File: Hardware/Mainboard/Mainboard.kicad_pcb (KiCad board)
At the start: 4 copper layers, 185.4 x 160 mm, 60 parts, among them IC1 TUSB2046BIRHBR, IC2 TUSB2046BIRHBR, IC3 TUSB2046BIRHBR, IC4 AOZ2261NQI-11, J1 Conn_02x10_Odd_Even, J10 Conn_02x03_Counter_Clockwise, J11 Conn_02x03_Counter_Clockwise, J12 ARJM11D7-009-AB-EW2, J13 USB4105-GF-A-060, J14 Conn_02x03_Odd_Even, J15 Conn_02x03_Odd_Even, J16 1844210, J17 Conn_02x03_Counter_Clockwise, J18 Conn_02x03_Counter_Clockwise, J19 Conn_02x03_Counter_Clockwise, J2 Conn_02x10_Odd_Even, J20 Conn_02x03_Counter_Clockwise, J21 Conn_02x03_Counter_Clockwise, J22 Conn_02x03_Counter_Clockwise, J23 Conn_02x03_Counter_Clockwise, J3 Conn_02x10_Odd_Even, J4 Conn_02x10_Odd_Even, J5 Conn_02x10_Odd_Even, J6 Conn_02x10_Odd_Even, J7 Conn_02x10_Odd_Even, J8 Conn_02x08_Odd_Even, J9 Conn_02x12_Odd_Even, P1 USB-A1HSW6, P2 USB-A1HSW6, SW1 SW_Push_Dual, SW2 SW_Push_Dual, SW3 SW_DPST, U1 ENC624J600-I/PT, U2 SC0915, U3 CD74HC154M96, U4 TCA9548A, U5 AZ1084CD-3.3TRG1, U6 AZ1084CD-3.3TRG1

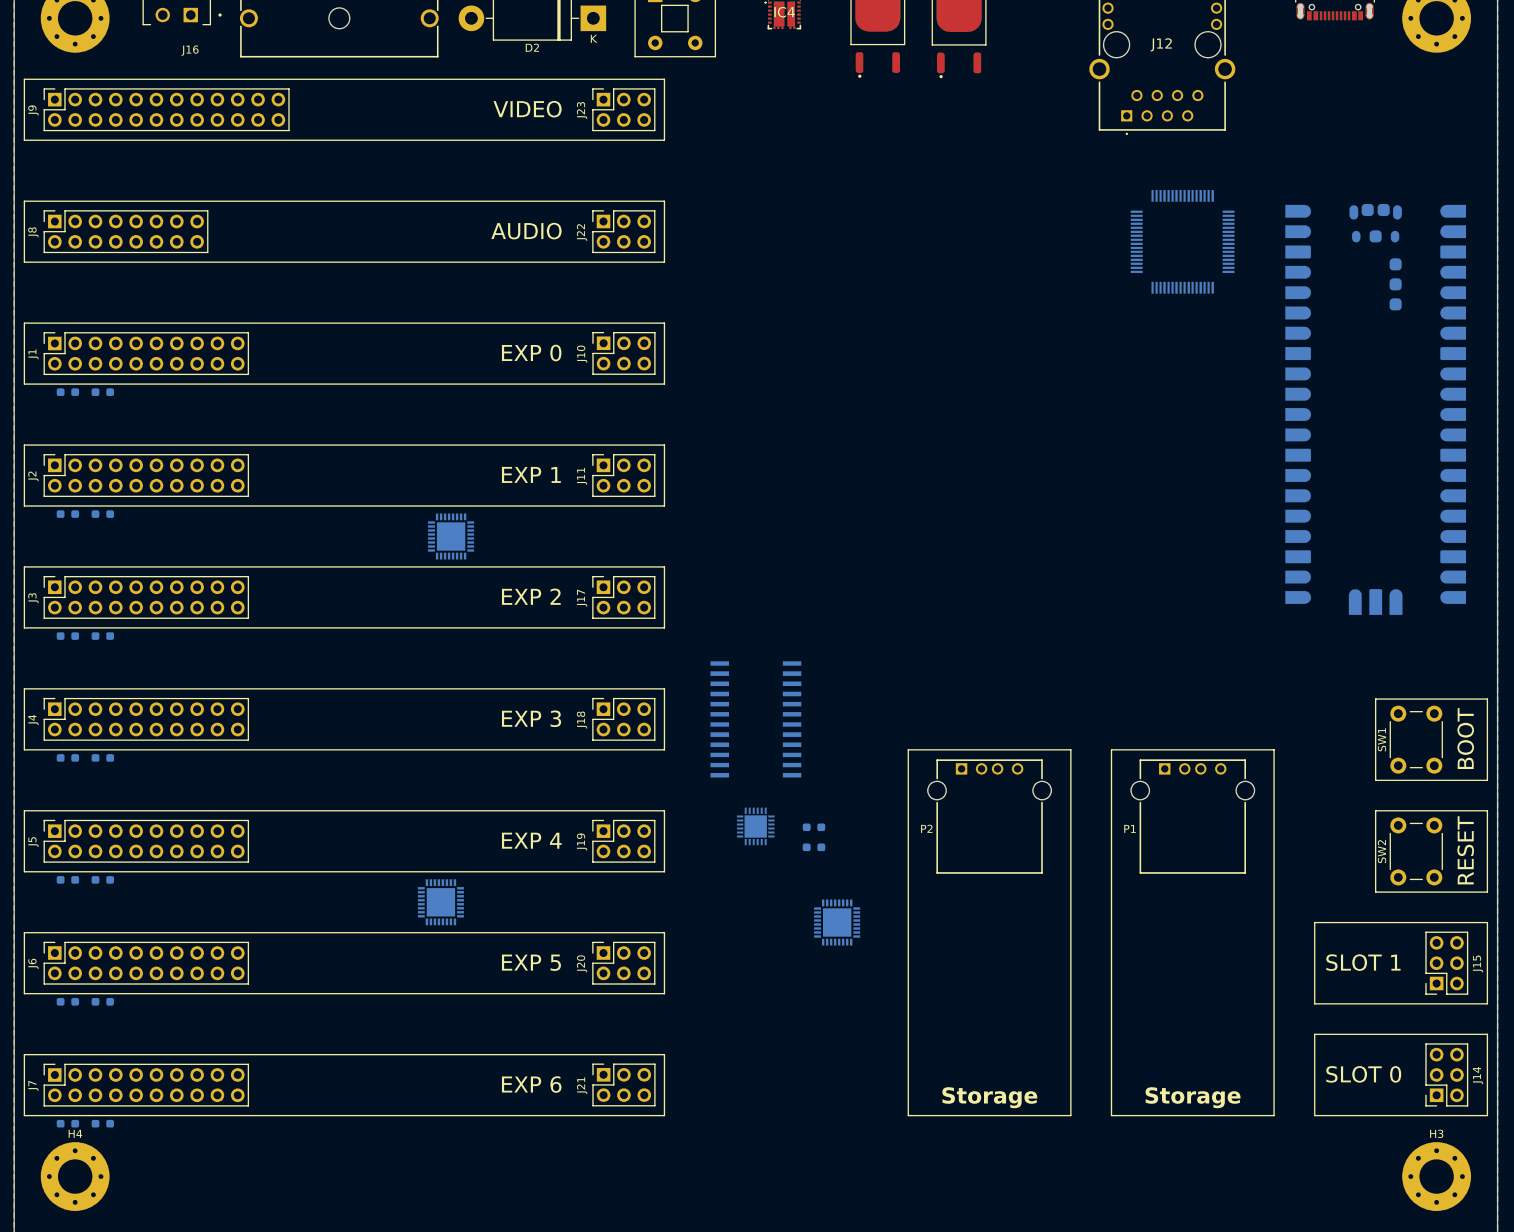
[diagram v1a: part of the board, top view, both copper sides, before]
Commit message: Adds RP2350 Stamp XL and dummy expansion board
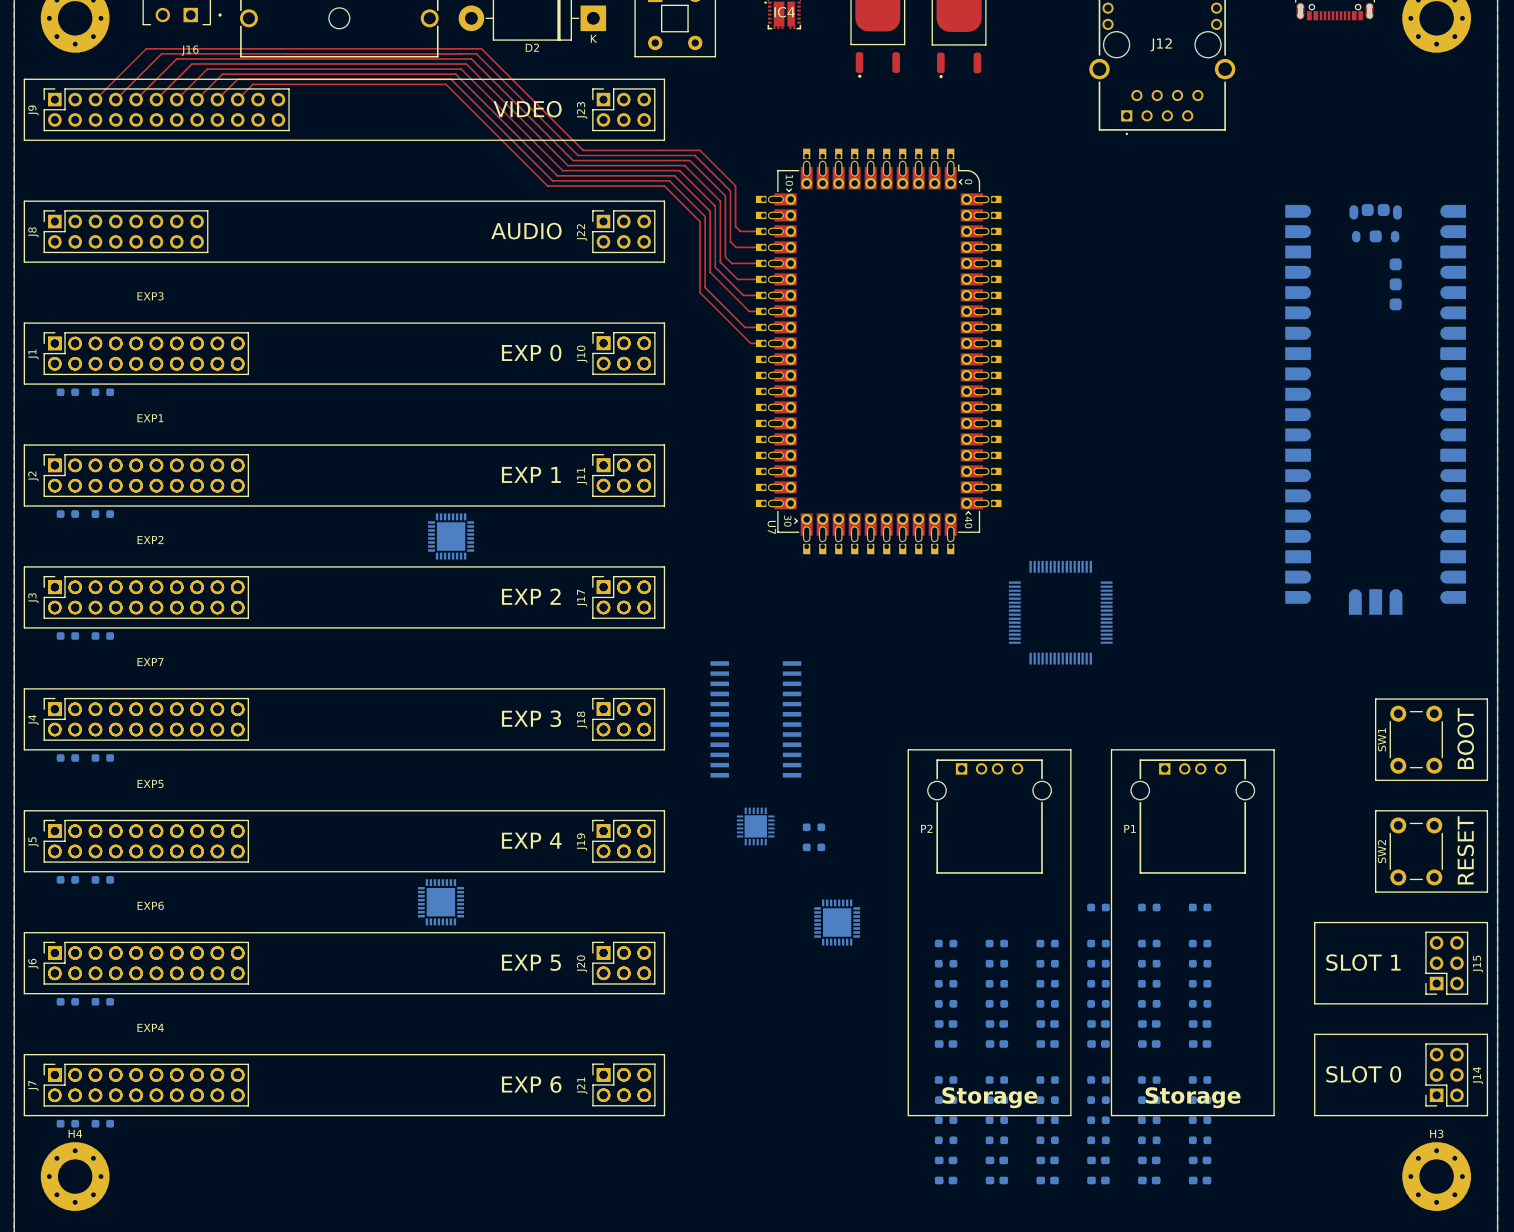
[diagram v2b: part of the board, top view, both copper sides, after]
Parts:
- added C1: 22pF, Capacitor_SMD:C_0603_1608Metric_Pad1.08x0.95mm_HandSolder, B.Cu at (159.7, 185.9)
- added C10: 22pF, Capacitor_SMD:C_0603_1608Metric_Pad1.08x0.95mm_HandSolder, B.Cu at (166.0, 166.3)
- added C11: 22pF, Capacitor_SMD:C_0603_1608Metric_Pad1.08x0.95mm_HandSolder, B.Cu at (191.4, 185.9)
- added C12: 22pF, Capacitor_SMD:C_0603_1608Metric_Pad1.08x0.95mm_HandSolder, B.Cu at (191.4, 183.4)
- added C13: 22pF, Capacitor_SMD:C_0603_1608Metric_Pad1.08x0.95mm_HandSolder, B.Cu at (185.1, 168.8)
- added C14: 22pF, Capacitor_SMD:C_0603_1608Metric_Pad1.08x0.95mm_HandSolder, B.Cu at (185.1, 166.3)
- added C15: 22pF, Capacitor_SMD:C_0603_1608Metric_Pad1.08x0.95mm_HandSolder, B.Cu at (166.0, 185.9)
- added C16: 22pF, Capacitor_SMD:C_0603_1608Metric_Pad1.08x0.95mm_HandSolder, B.Cu at (166.0, 183.4)
- added C17: 22pF, Capacitor_SMD:C_0603_1608Metric_Pad1.08x0.95mm_HandSolder, B.Cu at (185.1, 185.9)
- added C18: 22pF, Capacitor_SMD:C_0603_1608Metric_Pad1.08x0.95mm_HandSolder, B.Cu at (185.1, 183.4)
- added C19: 22pF, Capacitor_SMD:C_0603_1608Metric_Pad1.08x0.95mm_HandSolder, B.Cu at (178.7, 168.8)
- added C2: 22pF, Capacitor_SMD:C_0603_1608Metric_Pad1.08x0.95mm_HandSolder, B.Cu at (172.4, 168.8)
- added C20: 22pF, Capacitor_SMD:C_0603_1608Metric_Pad1.08x0.95mm_HandSolder, B.Cu at (178.7, 166.3)
- added C21: 22pF, Capacitor_SMD:C_0603_1608Metric_Pad1.08x0.95mm_HandSolder, B.Cu at (159.7, 168.8)
- added C22: 22pF, Capacitor_SMD:C_0603_1608Metric_Pad1.08x0.95mm_HandSolder, B.Cu at (159.7, 166.3)
- added C23: 22pF, Capacitor_SMD:C_0603_1608Metric_Pad1.08x0.95mm_HandSolder, B.Cu at (178.7, 185.9)
- added C24: 22pF, Capacitor_SMD:C_0603_1608Metric_Pad1.08x0.95mm_HandSolder, B.Cu at (178.7, 183.4)
- added C3: 22pF, Capacitor_SMD:C_0603_1608Metric_Pad1.08x0.95mm_HandSolder, B.Cu at (172.4, 185.9)
- added C4: 22pF, Capacitor_SMD:C_0603_1608Metric_Pad1.08x0.95mm_HandSolder, B.Cu at (159.7, 183.4)
- added C5: 22pF, Capacitor_SMD:C_0603_1608Metric_Pad1.08x0.95mm_HandSolder, B.Cu at (172.4, 166.3)
- added C6: 22pF, Capacitor_SMD:C_0603_1608Metric_Pad1.08x0.95mm_HandSolder, B.Cu at (172.4, 183.4)
- added C7: 22pF, Capacitor_SMD:C_0603_1608Metric_Pad1.08x0.95mm_HandSolder, B.Cu at (191.4, 168.8)
- added C8: 22pF, Capacitor_SMD:C_0603_1608Metric_Pad1.08x0.95mm_HandSolder, B.Cu at (191.4, 166.3)
- added C9: 22pF, Capacitor_SMD:C_0603_1608Metric_Pad1.08x0.95mm_HandSolder, B.Cu at (166.0, 168.8)
- added EXP1: ~, Home Computer:Expansion Card Preview, F.Cu at (59.7, 97.8)
- added EXP2: ~, Home Computer:Expansion Card Preview, F.Cu at (59.7, 113.0)
- added EXP3: ~, Home Computer:Expansion Card Preview, F.Cu at (59.7, 82.5)
- added EXP4: ~, Home Computer:Expansion Card Preview, F.Cu at (59.7, 174.0)
- added EXP5: ~, Home Computer:Expansion Card Preview, F.Cu at (59.7, 143.5)
- added EXP6: ~, Home Computer:Expansion Card Preview, F.Cu at (59.7, 158.7)
- added EXP7: ~, Home Computer:Expansion Card Preview, F.Cu at (59.7, 128.3)
- added R17: 10K, Resistor_SMD:R_0603_1608Metric_Pad0.98x0.95mm_HandSolder, B.Cu at (178.7, 151.8)
- added R18: 10K, Resistor_SMD:R_0603_1608Metric_Pad0.98x0.95mm_HandSolder, B.Cu at (191.4, 151.8)
- added R19: 10K, Resistor_SMD:R_0603_1608Metric_Pad0.98x0.95mm_HandSolder, B.Cu at (185.1, 151.8)
- added R20: 27, Resistor_SMD:R_0603_1608Metric_Pad0.98x0.95mm_HandSolder, B.Cu at (159.7, 180.9)
- added R21: 27, Resistor_SMD:R_0603_1608Metric_Pad0.98x0.95mm_HandSolder, B.Cu at (159.7, 178.4)
- added R22: 27, Resistor_SMD:R_0603_1608Metric_Pad0.98x0.95mm_HandSolder, B.Cu at (172.4, 163.8)
- added R23: 27, Resistor_SMD:R_0603_1608Metric_Pad0.98x0.95mm_HandSolder, B.Cu at (172.4, 161.3)
- added R24: 27, Resistor_SMD:R_0603_1608Metric_Pad0.98x0.95mm_HandSolder, B.Cu at (172.4, 180.9)
- added R25: 27, Resistor_SMD:R_0603_1608Metric_Pad0.98x0.95mm_HandSolder, B.Cu at (172.4, 178.4)
- added R26: 27, Resistor_SMD:R_0603_1608Metric_Pad0.98x0.95mm_HandSolder, B.Cu at (191.4, 163.8)
- added R27: 27, Resistor_SMD:R_0603_1608Metric_Pad0.98x0.95mm_HandSolder, B.Cu at (191.4, 161.3)
- added R28: 15K, Resistor_SMD:R_0603_1608Metric_Pad0.98x0.95mm_HandSolder, B.Cu at (191.4, 158.8)
- added R29: 15K, Resistor_SMD:R_0603_1608Metric_Pad0.98x0.95mm_HandSolder, B.Cu at (191.4, 156.3)
- added R30: 27, Resistor_SMD:R_0603_1608Metric_Pad0.98x0.95mm_HandSolder, B.Cu at (166.0, 163.8)
- added R31: 27, Resistor_SMD:R_0603_1608Metric_Pad0.98x0.95mm_HandSolder, B.Cu at (166.0, 161.3)
- added R32: 27, Resistor_SMD:R_0603_1608Metric_Pad0.98x0.95mm_HandSolder, B.Cu at (178.7, 163.8)
- added R33: 27, Resistor_SMD:R_0603_1608Metric_Pad0.98x0.95mm_HandSolder, B.Cu at (178.7, 161.3)
- added R34: 15K, Resistor_SMD:R_0603_1608Metric_Pad0.98x0.95mm_HandSolder, B.Cu at (178.7, 158.8)
- added R35: 15K, Resistor_SMD:R_0603_1608Metric_Pad0.98x0.95mm_HandSolder, B.Cu at (178.7, 156.3)
- added R36: 27, Resistor_SMD:R_0603_1608Metric_Pad0.98x0.95mm_HandSolder, B.Cu at (159.7, 163.8)
- added R37: 27, Resistor_SMD:R_0603_1608Metric_Pad0.98x0.95mm_HandSolder, B.Cu at (159.7, 161.3)
- added R38: 15K, Resistor_SMD:R_0603_1608Metric_Pad0.98x0.95mm_HandSolder, B.Cu at (159.7, 158.8)
- added R39: 15K, Resistor_SMD:R_0603_1608Metric_Pad0.98x0.95mm_HandSolder, B.Cu at (159.7, 156.3)
- added R40: 27, Resistor_SMD:R_0603_1608Metric_Pad0.98x0.95mm_HandSolder, B.Cu at (178.7, 180.9)
- added R41: 27, Resistor_SMD:R_0603_1608Metric_Pad0.98x0.95mm_HandSolder, B.Cu at (178.7, 178.4)
- added R42: 15K, Resistor_SMD:R_0603_1608Metric_Pad0.98x0.95mm_HandSolder, B.Cu at (178.7, 175.9)
- added R43: 15K, Resistor_SMD:R_0603_1608Metric_Pad0.98x0.95mm_HandSolder, B.Cu at (178.7, 173.4)
- added R44: 15K, Resistor_SMD:R_0603_1608Metric_Pad0.98x0.95mm_HandSolder, B.Cu at (159.7, 175.9)
- added R45: 15K, Resistor_SMD:R_0603_1608Metric_Pad0.98x0.95mm_HandSolder, B.Cu at (172.4, 158.8)
- added R46: 15K, Resistor_SMD:R_0603_1608Metric_Pad0.98x0.95mm_HandSolder, B.Cu at (172.4, 175.9)
- added R47: 15K, Resistor_SMD:R_0603_1608Metric_Pad0.98x0.95mm_HandSolder, B.Cu at (159.7, 173.4)
- added R48: 15K, Resistor_SMD:R_0603_1608Metric_Pad0.98x0.95mm_HandSolder, B.Cu at (172.4, 156.3)
- added R49: 15K, Resistor_SMD:R_0603_1608Metric_Pad0.98x0.95mm_HandSolder, B.Cu at (172.4, 173.4)
- added R50: 15K, Resistor_SMD:R_0603_1608Metric_Pad0.98x0.95mm_HandSolder, B.Cu at (166.0, 158.8)
- added R51: 15K, Resistor_SMD:R_0603_1608Metric_Pad0.98x0.95mm_HandSolder, B.Cu at (166.0, 156.3)
- added R52: 27, Resistor_SMD:R_0603_1608Metric_Pad0.98x0.95mm_HandSolder, B.Cu at (191.4, 180.9)
- added R53: 27, Resistor_SMD:R_0603_1608Metric_Pad0.98x0.95mm_HandSolder, B.Cu at (191.4, 178.4)
- added R54: 15K, Resistor_SMD:R_0603_1608Metric_Pad0.98x0.95mm_HandSolder, B.Cu at (191.4, 175.9)
- added R55: 15K, Resistor_SMD:R_0603_1608Metric_Pad0.98x0.95mm_HandSolder, B.Cu at (191.4, 173.4)
- added R56: 27, Resistor_SMD:R_0603_1608Metric_Pad0.98x0.95mm_HandSolder, B.Cu at (185.1, 163.8)
- added R57: 27, Resistor_SMD:R_0603_1608Metric_Pad0.98x0.95mm_HandSolder, B.Cu at (185.1, 161.3)
- added R58: 15K, Resistor_SMD:R_0603_1608Metric_Pad0.98x0.95mm_HandSolder, B.Cu at (185.1, 158.8)
- added R59: 15K, Resistor_SMD:R_0603_1608Metric_Pad0.98x0.95mm_HandSolder, B.Cu at (185.1, 156.3)
- added R60: 27, Resistor_SMD:R_0603_1608Metric_Pad0.98x0.95mm_HandSolder, B.Cu at (166.0, 180.9)
- added R61: 27, Resistor_SMD:R_0603_1608Metric_Pad0.98x0.95mm_HandSolder, B.Cu at (166.0, 178.4)
- added R62: 15K, Resistor_SMD:R_0603_1608Metric_Pad0.98x0.95mm_HandSolder, B.Cu at (166.0, 175.9)
- added R63: 15K, Resistor_SMD:R_0603_1608Metric_Pad0.98x0.95mm_HandSolder, B.Cu at (166.0, 173.4)
- added R64: 27, Resistor_SMD:R_0603_1608Metric_Pad0.98x0.95mm_HandSolder, B.Cu at (185.1, 180.9)
- added R65: 27, Resistor_SMD:R_0603_1608Metric_Pad0.98x0.95mm_HandSolder, B.Cu at (185.1, 178.4)
- added R66: 15K, Resistor_SMD:R_0603_1608Metric_Pad0.98x0.95mm_HandSolder, B.Cu at (185.1, 175.9)
- added R67: 15K, Resistor_SMD:R_0603_1608Metric_Pad0.98x0.95mm_HandSolder, B.Cu at (185.1, 173.4)
- added U7: RP2350_Stamp_XL, RP2xxx_Stamp:RP2xxx_Stamp_XL_FlexyPin, F.Cu at (151.2, 82.3)
- moved U1 48.8 mm to (174.0, 114.9), turned to 90 degrees
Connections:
- IC1 pad 10: unconnected-(IC1-~{OVRCUR}-Pad10) -> +3V3
- IC1 pad 11: /Expansion Subsystem/USB0_{D-} -> /Expansion Subsystem/USB Hub x5/USB Terminator3/HUB_{D-}
- IC1 pad 12: /Expansion Subsystem/USB0_{D+} -> /Expansion Subsystem/USB Hub x5/USB Terminator3/HUB_{D+}
- IC1 pad 14: unconnected-(IC1-~{OVRCUR2}-Pad14) -> +3V3
- IC1 pad 15: /Expansion Subsystem/USB1_{D-} -> /Expansion Subsystem/USB Hub x5/USB Terminator2/HUB_{D-}
- IC1 pad 16: /Expansion Subsystem/USB1_{D+} -> /Expansion Subsystem/USB Hub x5/USB Terminator2/HUB_{D+}
- IC1 pad 18: unconnected-(IC1-~{OVRCUR3}-Pad18) -> +3V3
- IC1 pad 19: /Expansion Subsystem/USB2_{D-} -> /Expansion Subsystem/USB Hub x5/USB Terminator1/HUB_{D-}
- IC1 pad 20: /Expansion Subsystem/USB2_{D+} -> /Expansion Subsystem/USB Hub x5/USB Terminator1/HUB_{D+}
- IC1 pad 22: unconnected-(IC1-~{OVRCUR4}-Pad22) -> +3V3
- IC1 pad 23: /Expansion Subsystem/USB3_{D-} -> /Expansion Subsystem/USB Hub x5/USB Terminator/HUB_{D-}
- IC1 pad 24: /Expansion Subsystem/USB3_{D+} -> /Expansion Subsystem/USB Hub x5/USB Terminator/HUB_{D+}
- IC1 pad 25: unconnected-(IC1-VCC_2-Pad25) -> +3V3
- IC1 pad 26: unconnected-(IC1-~{EXTMEM}-Pad26) -> +3V3
- IC1 pad 28: unconnected-(IC1-GND_2-Pad28) -> GND
- IC1 pad 3: unconnected-(IC1-VCC_1-Pad3) -> +3V3
- IC1 pad 33: unconnected-(IC1-EP-Pad33) -> GND
- IC1 pad 4: unconnected-(IC1-~{RESET}-Pad4) -> /Expansion Subsystem/USB Hub x5/~{RESET}
- IC1 pad 6: unconnected-(IC1-EEDATA/GANGED-Pad6) -> GND
- IC1 pad 7: unconnected-(IC1-GND_1-Pad7) -> GND
- IC1 pad 8: unconnected-(IC1-BUSPWR-Pad8) -> GND
- IC2 pad 10: unconnected-(IC2-~{OVRCUR}-Pad10) -> +3V3
- IC2 pad 11: /Expansion Subsystem/D0_{D+} -> /USB Subsystem/USB Hub x4/USB Terminator3/HUB_{D-}
- IC2 pad 12: /Expansion Subsystem/D0_{D-} -> /USB Subsystem/USB Hub x4/USB Terminator3/HUB_{D+}
- IC2 pad 14: unconnected-(IC2-~{OVRCUR2}-Pad14) -> +3V3
- IC2 pad 15: /Expansion Subsystem/D1_{D+} -> /USB Subsystem/USB Hub x4/USB Terminator2/HUB_{D-}
- IC2 pad 16: /USB Subsystem/D1_{D-} -> /USB Subsystem/USB Hub x4/USB Terminator2/HUB_{D+}
- IC2 pad 18: unconnected-(IC2-~{OVRCUR3}-Pad18) -> +3V3
- IC2 pad 19: /USB Subsystem/D2_{D-} -> /USB Subsystem/USB Hub x4/USB Terminator1/HUB_{D-}
- IC2 pad 20: /USB Subsystem/D2_{D+} -> /USB Subsystem/USB Hub x4/USB Terminator1/HUB_{D+}
- IC2 pad 22: unconnected-(IC2-~{OVRCUR4}-Pad22) -> +3V3
- IC2 pad 23: /USB Subsystem/D3_{D-} -> /USB Subsystem/USB Hub x4/USB Terminator/HUB_{D-}
- IC2 pad 24: /USB Subsystem/D3_{D+} -> /USB Subsystem/USB Hub x4/USB Terminator/HUB_{D+}
- IC2 pad 25: unconnected-(IC2-VCC_2-Pad25) -> +3V3
- IC2 pad 26: unconnected-(IC2-~{EXTMEM}-Pad26) -> +3V3
- IC2 pad 28: unconnected-(IC2-GND_2-Pad28) -> GND
- IC2 pad 3: unconnected-(IC2-VCC_1-Pad3) -> +3V3
- IC2 pad 33: unconnected-(IC2-EP-Pad33) -> GND
- IC2 pad 4: unconnected-(IC2-~{RESET}-Pad4) -> /USB Subsystem/USB Hub x4/~{RESET}
- IC2 pad 6: unconnected-(IC2-EEDATA/GANGED-Pad6) -> GND
- IC2 pad 7: unconnected-(IC2-GND_1-Pad7) -> GND
- IC2 pad 8: unconnected-(IC2-BUSPWR-Pad8) -> GND
- IC3 pad 10: unconnected-(IC3-~{OVRCUR}-Pad10) -> +3V3
- IC3 pad 11: /Expansion Subsystem/USB4_{D-} -> /Expansion Subsystem/USB Hub x6/USB Terminator3/HUB_{D-}
- IC3 pad 12: /Expansion Subsystem/USB4_{D+} -> /Expansion Subsystem/USB Hub x6/USB Terminator3/HUB_{D+}
- IC3 pad 14: unconnected-(IC3-~{OVRCUR2}-Pad14) -> +3V3
- IC3 pad 15: /Expansion Subsystem/USB5_{D-} -> /Expansion Subsystem/USB Hub x6/USB Terminator2/HUB_{D-}
- IC3 pad 16: /Expansion Subsystem/USB5_{D+} -> /Expansion Subsystem/USB Hub x6/USB Terminator2/HUB_{D+}
- IC3 pad 18: unconnected-(IC3-~{OVRCUR3}-Pad18) -> +3V3
- IC3 pad 19: /Expansion Subsystem/USB6_{D-} -> /Expansion Subsystem/USB Hub x6/USB Terminator1/HUB_{D-}
- IC3 pad 20: /Expansion Subsystem/USB6_{D+} -> /Expansion Subsystem/USB Hub x6/USB Terminator1/HUB_{D+}
- IC3 pad 22: unconnected-(IC3-~{OVRCUR4}-Pad22) -> +3V3
- IC3 pad 23: /Expansion Subsystem/USB Hub x6/D3_{D-} -> /Expansion Subsystem/USB Hub x6/USB Terminator/HUB_{D-}
- IC3 pad 24: /Expansion Subsystem/USB Hub x6/D3_{D+} -> /Expansion Subsystem/USB Hub x6/USB Terminator/HUB_{D+}
- IC3 pad 25: unconnected-(IC3-VCC_2-Pad25) -> +3V3
- IC3 pad 26: unconnected-(IC3-~{EXTMEM}-Pad26) -> +3V3
- IC3 pad 28: unconnected-(IC3-GND_2-Pad28) -> GND
- IC3 pad 3: unconnected-(IC3-VCC_1-Pad3) -> +3V3
- IC3 pad 33: unconnected-(IC3-EP-Pad33) -> GND
- IC3 pad 4: unconnected-(IC3-~{RESET}-Pad4) -> /Expansion Subsystem/USB Hub x6/~{RESET}
- IC3 pad 6: unconnected-(IC3-EEDATA/GANGED-Pad6) -> GND
- IC3 pad 7: unconnected-(IC3-GND_1-Pad7) -> GND
- IC3 pad 8: unconnected-(IC3-BUSPWR-Pad8) -> GND
- J14 pad 1: /OnBoard Peripherials/I2C_{SCL} -> /SYS_{SCL}
- J14 pad 3: /OnBoard Peripherials/I2C_{SDA} -> /SYS_{SDA}
- J15 pad 1: /OnBoard Peripherials/I2C_{SCL} -> /SYS_{SCL}
- J15 pad 3: /OnBoard Peripherials/I2C_{SDA} -> /SYS_{SDA}
- J8 pad 10: /Audio Subsystem/I2S_{SCK} -> /I2S_{SCK}
- J8 pad 12: /Audio Subsystem/I2S_{OUT} -> /I2S_{OUT}
- J8 pad 14: /Audio Subsystem/I2S_{IN} -> /I2S_{IN}
- J8 pad 4: /Audio Subsystem/I2S_{MCK} -> /I2S_{MCK}
- J8 pad 8: /Audio Subsystem/I2S_{LRCK} -> /I2S_{LRCK}
- J9 pad 11: /Video Subsystem/HSTX_{3} -> /HSTX_{3}
- J9 pad 13: /Video Subsystem/HSTX_{4} -> /HSTX_{4}
- J9 pad 15: /Video Subsystem/HSTX_{5} -> /HSTX_{5}
- J9 pad 17: /Video Subsystem/HSTX_{6} -> /HSTX_{6}
- J9 pad 19: /Video Subsystem/HSTX_{7} -> /HSTX_{7}
- J9 pad 2: /Video Subsystem/DDC_{SCL} -> /SYS_{SCL}
- J9 pad 4: /Video Subsystem/DDC_{SDA} -> /SYS_{SDA}
- J9 pad 5: /Video Subsystem/HSTX_{0} -> /HSTX_{0}
- J9 pad 7: /Video Subsystem/HSTX_{1} -> /HSTX_{1}
- J9 pad 9: /Video Subsystem/HSTX_{2} -> /HSTX_{2}
- R15 pad 2: /OnBoard Peripherials/I2C_{SDA} -> /SYS_{SDA}
- R16 pad 2: /OnBoard Peripherials/I2C_{SCL} -> /SYS_{SCL}
- U1 pad 34: /Ethernet/~{IRQ} -> /~{IRQ_{ETH}}
- U2 pad 6: /Debug Subsystem/PROBE_RXD -> /DBG_{RXD}
- U2 pad 7: /Debug Subsystem/PROBE_TXD -> /DBG_{TXD}
- U4 pad 16: /OnBoard Peripherials/I2C_{SDA} -> /SYS_{SDA}
- U4 pad 17: /OnBoard Peripherials/I2C_{SCL} -> /SYS_{SCL}
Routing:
- net /HSTX_{0}: track 0.00 -> 98.6 mm
- net /HSTX_{1}: track 0.00 -> 97.1 mm
- net /HSTX_{2}: track 0.00 -> 95.6 mm
- net /HSTX_{3}: track 0.00 -> 93.3 mm
- net /HSTX_{4}: track 0.00 -> 91.1 mm
- net /HSTX_{5}: track 0.00 -> 88.9 mm
- net /HSTX_{6}: track 0.00 -> 87.4 mm
- net /HSTX_{7}: track 0.00 -> 85.1 mm

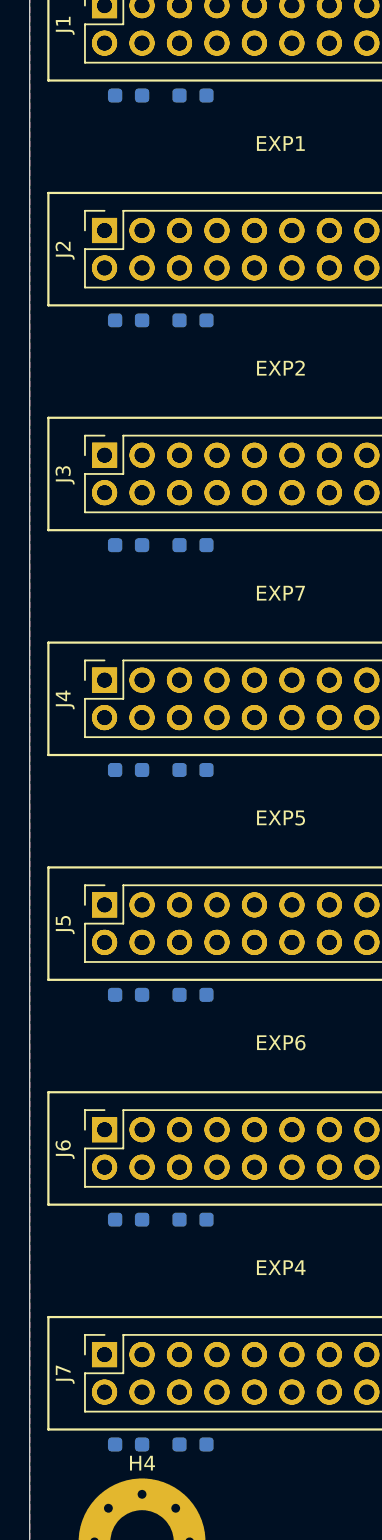
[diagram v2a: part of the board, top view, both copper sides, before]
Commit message: Adds pull-ups and irq controller to expansion subsystem
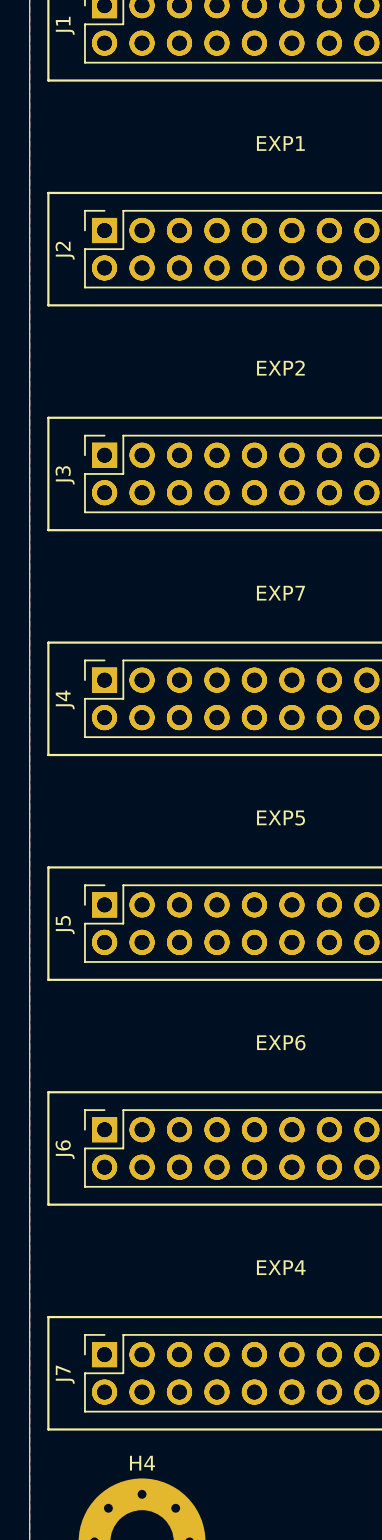
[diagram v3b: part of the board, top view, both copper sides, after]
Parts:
- removed R1, R10, R11, R12, R13, R14, R2, R3, R4, R5, R6, R7, R8, R9: 10K, Resistor_SMD:R_0603_1608Metric_Pad0.98x0.95mm_HandSolder
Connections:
- J1 pad 4: /Expansion Subsystem/I2C0_{SCL} -> /Expansion Subsystem/Expansion Port0/I2C_{SCL}
- J1 pad 6: /Expansion Subsystem/I2C0_{SDA} -> /Expansion Subsystem/Expansion Port0/I2C_{SDA}
- J2 pad 4: /Expansion Subsystem/I2C1_{SCL} -> /Expansion Subsystem/Expansion Port1/I2C_{SCL}
- J2 pad 6: /Expansion Subsystem/I2C1_{SDA} -> /Expansion Subsystem/Expansion Port1/I2C_{SDA}
- J3 pad 4: /Expansion Subsystem/I2C2_{SCL} -> /Expansion Subsystem/Expansion Port2/I2C_{SCL}
- J3 pad 6: /Expansion Subsystem/I2C2_{SDA} -> /Expansion Subsystem/Expansion Port2/I2C_{SDA}
- J4 pad 4: /Expansion Subsystem/I2C3_{SCL} -> /Expansion Subsystem/Expansion Port3/I2C_{SCL}
- J4 pad 6: /Expansion Subsystem/I2C3_{SDA} -> /Expansion Subsystem/Expansion Port3/I2C_{SDA}
- J5 pad 4: /Expansion Subsystem/I2C4_{SCL} -> /Expansion Subsystem/Expansion Port4/I2C_{SCL}
- J5 pad 6: /Expansion Subsystem/I2C4_{SDA} -> /Expansion Subsystem/Expansion Port4/I2C_{SDA}
- J6 pad 4: /Expansion Subsystem/I2C5_{SCL} -> /Expansion Subsystem/Expansion Port5/I2C_{SCL}
- J6 pad 6: /Expansion Subsystem/I2C5_{SDA} -> /Expansion Subsystem/Expansion Port5/I2C_{SDA}
- J7 pad 4: /Expansion Subsystem/I2C6_{SCL} -> /Expansion Subsystem/Expansion Port6/I2C_{SCL}
- J7 pad 6: /Expansion Subsystem/I2C6_{SDA} -> /Expansion Subsystem/Expansion Port6/I2C_{SDA}
- U3 pad 17: /Expansion Subsystem/SPI_{CS14} -> /Expansion Subsystem/SPI_{CS13}
